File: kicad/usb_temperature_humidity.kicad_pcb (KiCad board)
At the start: 2 copper layers, 72 x 47 mm, 22 parts, among them J1 Conn_01x01, J10 Conn_01x01, J11 Conn_01x01, J12 Conn_01x01, J13 Conn_01x01, J14 Conn_01x01, J2 Conn_01x01, J3 Conn_01x01, J4 Conn_01x01, J5 Conn_01x01, J6 Conn_01x01, J7 Conn_01x01, J8 Conn_01x01, J9 Conn_01x01, SW1 SW_SPDT, SW2 SW_SPDT, U1 SeeeduinoXIAO, U2 SHT-31

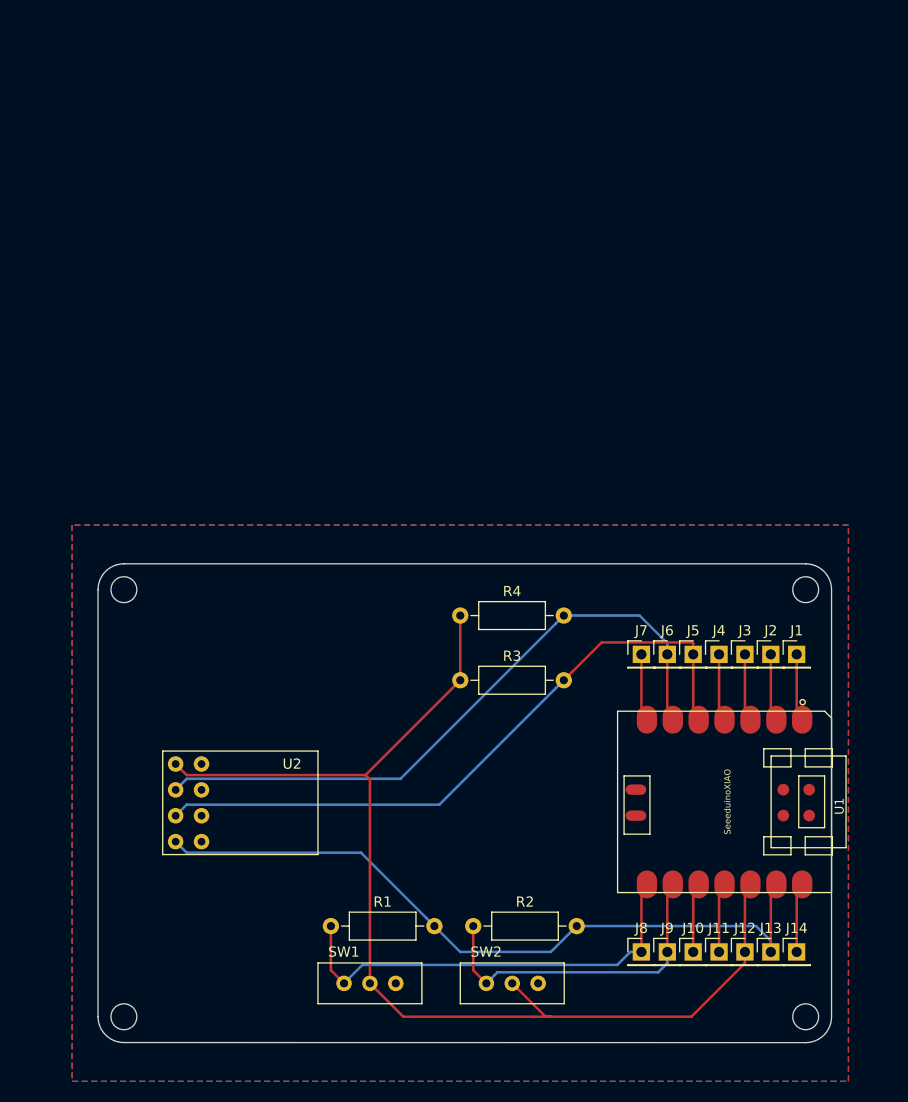
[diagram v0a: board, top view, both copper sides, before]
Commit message: 基板外形を秋月Cタイプ基板に合わせた
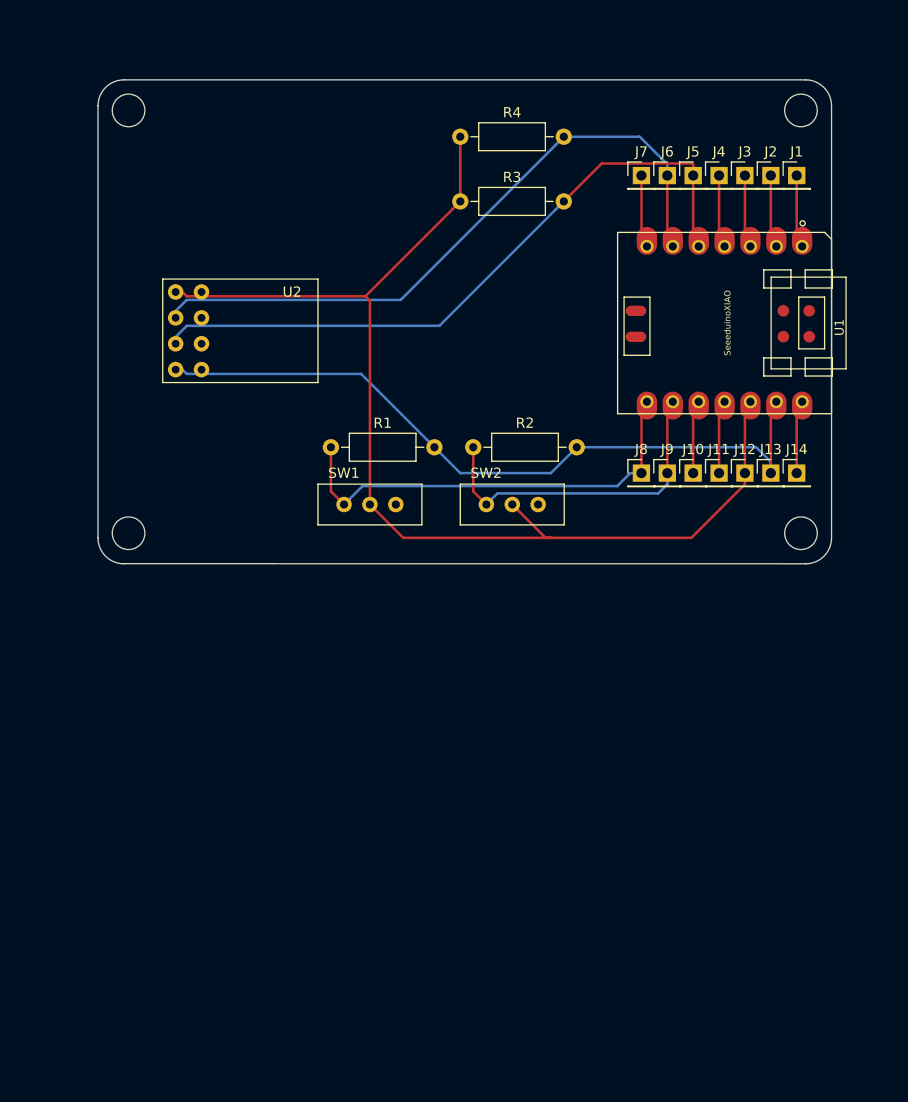
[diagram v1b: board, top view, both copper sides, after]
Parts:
- SW1, SW2: footprint Mylib:SW_SLIDE_sengoku -> kicad_mylib:SW_SLIDE_sengoku
- U1: footprint Seeeduino XIAO:Seeeduino XIAO-MOUDLE14P-2.54-21X17.8MM -> kicad_mylib:SeeedXIAO
- U2: footprint SHT-31:SHT-31 -> kicad_mylib:SHT-31
- moved J1 47.0 mm to (68.6, -38.1)
- moved J10 47.0 mm to (58.4, -8.90)
- moved J11 47.0 mm to (61.0, -8.90)
- moved J12 47.0 mm to (63.5, -8.90)
- moved J13 47.0 mm to (66.0, -8.90)
- moved J14 47.0 mm to (68.6, -8.90)
- moved J2 47.0 mm to (66.0, -38.1)
- moved J3 47.0 mm to (63.5, -38.1)
- moved J4 47.0 mm to (61.0, -38.1)
- moved J5 47.0 mm to (58.4, -38.1)
- moved J6 47.0 mm to (55.9, -38.1)
- moved J7 47.0 mm to (53.3, -38.1)
- moved J8 47.0 mm to (53.3, -8.90)
- moved J9 47.0 mm to (55.9, -8.90)
- moved R1 47.0 mm to (22.9, -11.4)
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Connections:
- U2 pad 5: Net-(U2-Pad5) -> GND
- U2 pad 6: Net-(U2-Pad6) -> GND
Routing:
- removed copper zone on B.Cu, net GND
- removed copper zone on F.Cu, net GND
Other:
- board size 72 x 47 mm -> 72 x 47.5 mm

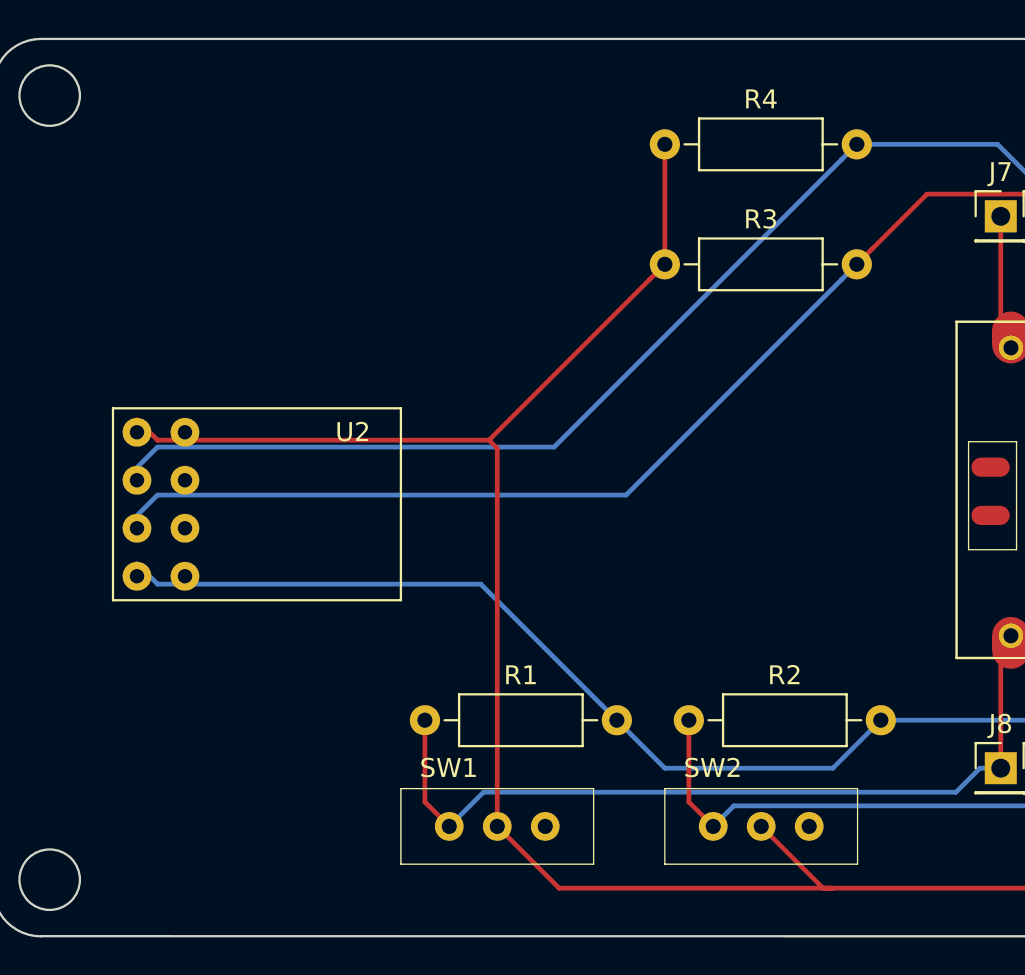
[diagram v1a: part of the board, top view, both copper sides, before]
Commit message: 抵抗の容量をシルクに記載した
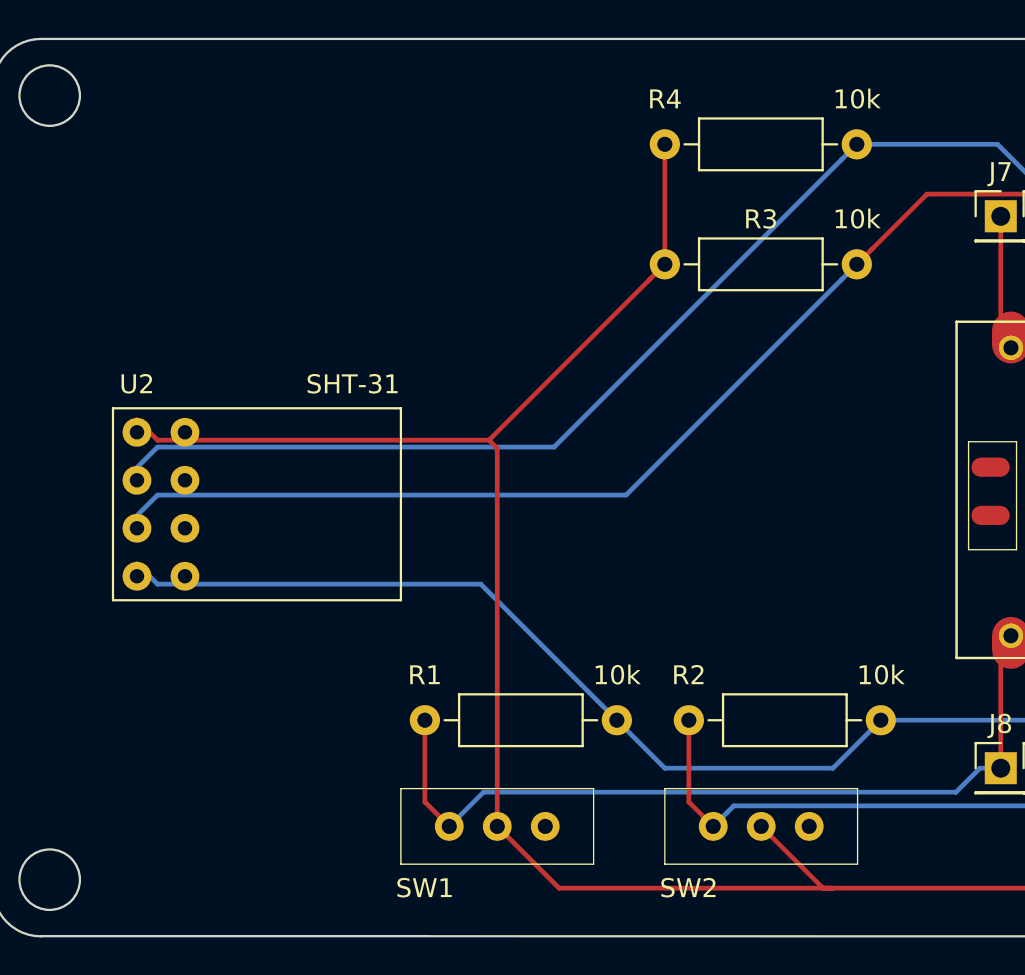
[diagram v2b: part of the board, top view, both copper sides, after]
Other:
- board text added: "10k"
- board text added: "SHT-31"
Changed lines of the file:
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@@
   (general
     (thickness 1.6)
-    (drawings 12)
+    (drawings 17)
     (tracks 81)
     (zones 0)
@@
   (module kicad_mylib:SHT-31 (layer F.Cu)
     (at 6.35 -17.79)
-    (fp_text reference U2 (at 12.7 -8.89) (layer F.SilkS)
+    (fp_text reference U2 (at 1.27 -11.42) (layer F.SilkS)
       (effects (font (size 1 1) (thickness 0.15)))
     )
@@
   (module kicad_mylib:SW_SLIDE_sengoku (layer F.Cu)
     (at 35.56 -3.82)
-    (fp_text reference SW2 (at 2.54 -5.08) (layer F.SilkS)
+    (fp_text reference SW2 (at 1.27 1.28) (layer F.SilkS)
       (effects (font (size 1 1) (thickness 0.15)))
     )
@@
   (module kicad_mylib:SW_SLIDE_sengoku (layer F.Cu)
     (at 21.59 -3.82)
-    (fp_text reference SW1 (at 2.54 -5.08) (layer F.SilkS)
+    (fp_text reference SW1 (at 1.27 1.28) (layer F.SilkS)
       (effects (font (size 1 1) (thickness 0.15)))
     )
@@
     (descr "Resistor, Axial_DIN0207 series, Axial, Horizontal, pin pitch=10.16mm, 0.25W = 1/4W, length*diameter=6.3*2.5mm^2, http://cdn-reichelt.de/documents/datenblatt/B400/1_4W%23YAG.pdf")
     (tags "Resistor Axial_DIN0207 series Axial Horizontal pin pitch 10.16mm 0.25W = 1/4W length 6.3mm diameter 2.5mm")
-    (fp_text reference R4 (at 5.08 -2.37) (layer F.SilkS)
+    (fp_text reference R4 (at 0 -2.37) (layer F.SilkS)
       (effects (font (size 1 1) (thickness 0.15)))
     )
@@
     (descr "Resistor, Axial_DIN0207 series, Axial, Horizontal, pin pitch=10.16mm, 0.25W = 1/4W, length*diameter=6.3*2.5mm^2, http://cdn-reichelt.de/documents/datenblatt/B400/1_4W%23YAG.pdf")
     (tags "Resistor Axial_DIN0207 series Axial Horizontal pin pitch 10.16mm 0.25W = 1/4W length 6.3mm diameter 2.5mm")
-    (fp_text reference R1 (at 5.08 -2.37) (layer F.SilkS)
+    (fp_text reference R1 (at 0 -2.37) (layer F.SilkS)
       (effects (font (size 1 1) (thickness 0.15)))
     )
@@
     (descr "Resistor, Axial_DIN0207 series, Axial, Horizontal, pin pitch=10.16mm, 0.25W = 1/4W, length*diameter=6.3*2.5mm^2, http://cdn-reichelt.de/documents/datenblatt/B400/1_4W%23YAG.pdf")
     (tags "Resistor Axial_DIN0207 series Axial Horizontal pin pitch 10.16mm 0.25W = 1/4W length 6.3mm diameter 2.5mm")
-    (fp_text reference R2 (at 5.08 -2.37) (layer F.SilkS)
+    (fp_text reference R2 (at 0 -2.37) (layer F.SilkS)
       (effects (font (size 1 1) (thickness 0.15)))
     )
@@
     )
   )
+  (gr_text SHT-31 (at 19.05 -29.21) (layer F.SilkS)
+    (effects (font (size 1 1) (thickness 0.15)))
+  )
+  (gr_text 10k (at 45.72 -37.94) (layer F.SilkS)
+    (effects (font (size 1 1) (thickness 0.15)))
+  )
+  (gr_text 10k (at 45.72 -44.29) (layer F.SilkS)
+    (effects (font (size 1 1) (thickness 0.15)))
+  )
+  (gr_text 10k (at 46.99 -13.81) (layer F.SilkS)
+    (effects (font (size 1 1) (thickness 0.15)))
+  )
+  (gr_text 10k (at 33.02 -13.81) (layer F.SilkS)
+    (effects (font (size 1 1) (thickness 0.15)))
+  )
   (gr_line (start 2.54 -47.5) (end 69.46 -47.5) (layer Edge.Cuts) (width 0.12))

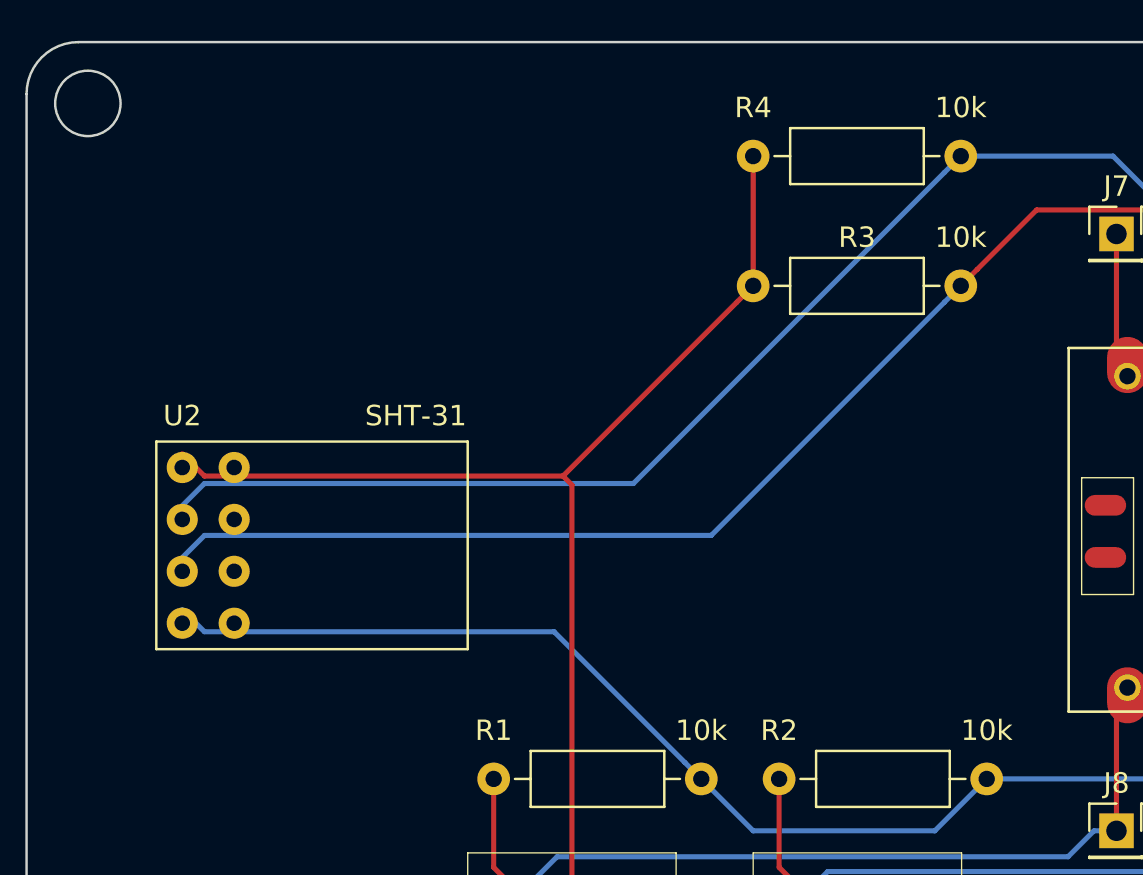
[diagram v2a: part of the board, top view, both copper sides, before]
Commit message: SHT-31の1ピンにシルクでマークをつけた
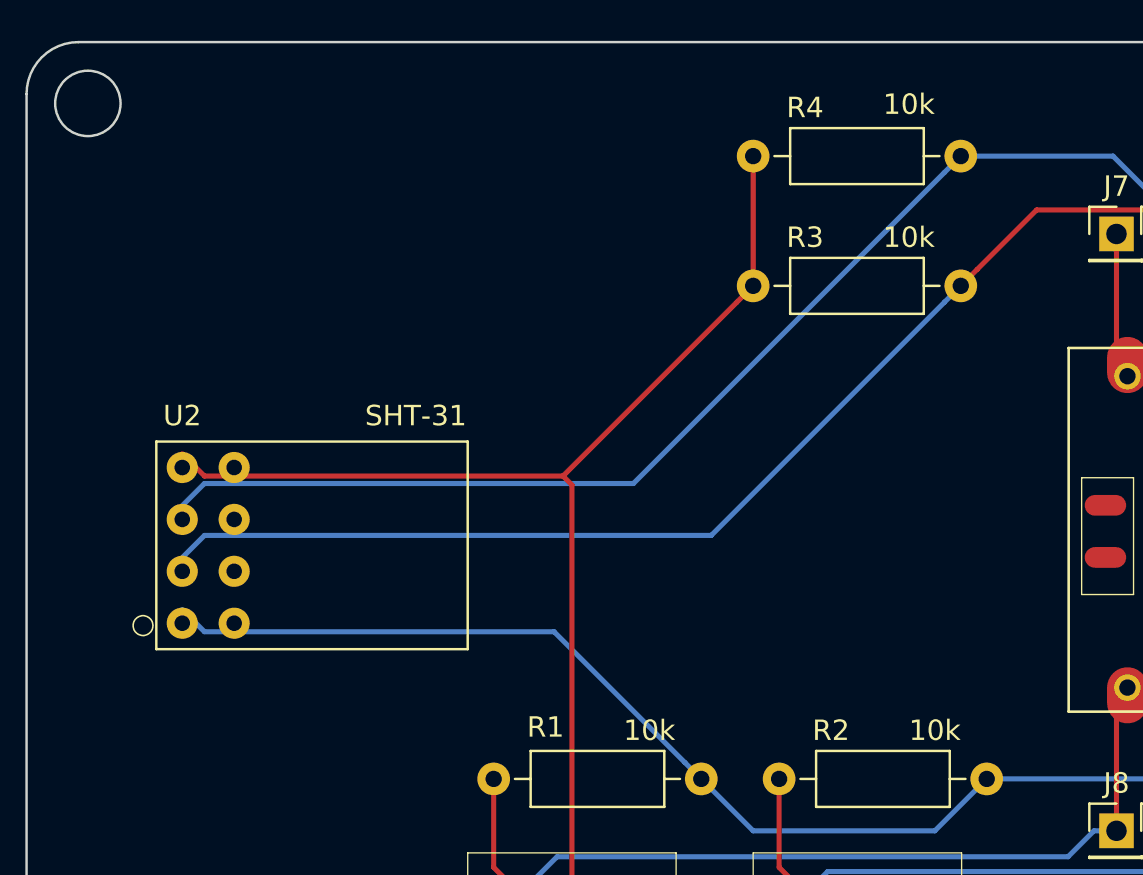
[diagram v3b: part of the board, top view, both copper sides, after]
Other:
- board text added: "○"
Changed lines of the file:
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@@
   (general
     (thickness 1.6)
-    (drawings 17)
+    (drawings 18)
     (tracks 81)
     (zones 0)
@@
     (descr "Resistor, Axial_DIN0207 series, Axial, Horizontal, pin pitch=10.16mm, 0.25W = 1/4W, length*diameter=6.3*2.5mm^2, http://cdn-reichelt.de/documents/datenblatt/B400/1_4W%23YAG.pdf")
     (tags "Resistor Axial_DIN0207 series Axial Horizontal pin pitch 10.16mm 0.25W = 1/4W length 6.3mm diameter 2.5mm")
-    (fp_text reference R4 (at 0 -2.37) (layer F.SilkS)
+    (fp_text reference R4 (at 2.54 -2.37) (layer F.SilkS)
       (effects (font (size 1 1) (thickness 0.15)))
     )
@@
     (descr "Resistor, Axial_DIN0207 series, Axial, Horizontal, pin pitch=10.16mm, 0.25W = 1/4W, length*diameter=6.3*2.5mm^2, http://cdn-reichelt.de/documents/datenblatt/B400/1_4W%23YAG.pdf")
     (tags "Resistor Axial_DIN0207 series Axial Horizontal pin pitch 10.16mm 0.25W = 1/4W length 6.3mm diameter 2.5mm")
-    (fp_text reference R3 (at 5.08 -2.37) (layer F.SilkS)
+    (fp_text reference R3 (at 2.54 -2.37) (layer F.SilkS)
       (effects (font (size 1 1) (thickness 0.15)))
     )
@@
     (descr "Resistor, Axial_DIN0207 series, Axial, Horizontal, pin pitch=10.16mm, 0.25W = 1/4W, length*diameter=6.3*2.5mm^2, http://cdn-reichelt.de/documents/datenblatt/B400/1_4W%23YAG.pdf")
     (tags "Resistor Axial_DIN0207 series Axial Horizontal pin pitch 10.16mm 0.25W = 1/4W length 6.3mm diameter 2.5mm")
-    (fp_text reference R1 (at 0 -2.37) (layer F.SilkS)
+    (fp_text reference R1 (at 2.54 -2.53) (layer F.SilkS)
       (effects (font (size 1 1) (thickness 0.15)))
     )
@@
     (descr "Resistor, Axial_DIN0207 series, Axial, Horizontal, pin pitch=10.16mm, 0.25W = 1/4W, length*diameter=6.3*2.5mm^2, http://cdn-reichelt.de/documents/datenblatt/B400/1_4W%23YAG.pdf")
     (tags "Resistor Axial_DIN0207 series Axial Horizontal pin pitch 10.16mm 0.25W = 1/4W length 6.3mm diameter 2.5mm")
-    (fp_text reference R2 (at 0 -2.37) (layer F.SilkS)
+    (fp_text reference R2 (at 2.54 -2.37) (layer F.SilkS)
       (effects (font (size 1 1) (thickness 0.15)))
     )
@@
     )
   )
+  (gr_text ○ (at 5.7 -19.05) (layer F.SilkS)
+    (effects (font (size 1 1) (thickness 0.15)))
+  )
   (gr_text SHT-31 (at 19.05 -29.21) (layer F.SilkS)
     (effects (font (size 1 1) (thickness 0.15)))
   )
-  (gr_text 10k (at 45.72 -37.94) (layer F.SilkS)
+  (gr_text 10k (at 43.18 -37.94) (layer F.SilkS)
     (effects (font (size 1 1) (thickness 0.15)))
   )
-  (gr_text 10k (at 45.72 -44.29) (layer F.SilkS)
+  (gr_text 10k (at 43.18 -44.45) (layer F.SilkS)
     (effects (font (size 1 1) (thickness 0.15)))
   )
-  (gr_text 10k (at 46.99 -13.81) (layer F.SilkS)
+  (gr_text 10k (at 44.45 -13.81) (layer F.SilkS)
     (effects (font (size 1 1) (thickness 0.15)))
   )
-  (gr_text 10k (at 33.02 -13.81) (layer F.SilkS)
+  (gr_text 10k (at 30.48 -13.81) (layer F.SilkS)
     (effects (font (size 1 1) (thickness 0.15)))
   )
